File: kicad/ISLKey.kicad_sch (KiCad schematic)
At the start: 43 parts, among them J10 5-60V AC/DC IN, J11 12V OUT (lock/aux), J13 TTGO batt pads, J3 Exit btn, J4 Door contact, J5 Tamper, J6 LOCK COM/NO/NC, J7 AUX COM/NO/NC, J8 Fire volt-free, J9 Fire link COM-Fire, K1 SRD-05VDC-SL-C, K2 SRD-05VDC-SL-C, M1 TTGO T-Display, Q1 PN2222A, Q2 PN2222A, U1 PC817, U3 TEN20-2412WIN, U4 TSR-1-2450, U5 DS3231M

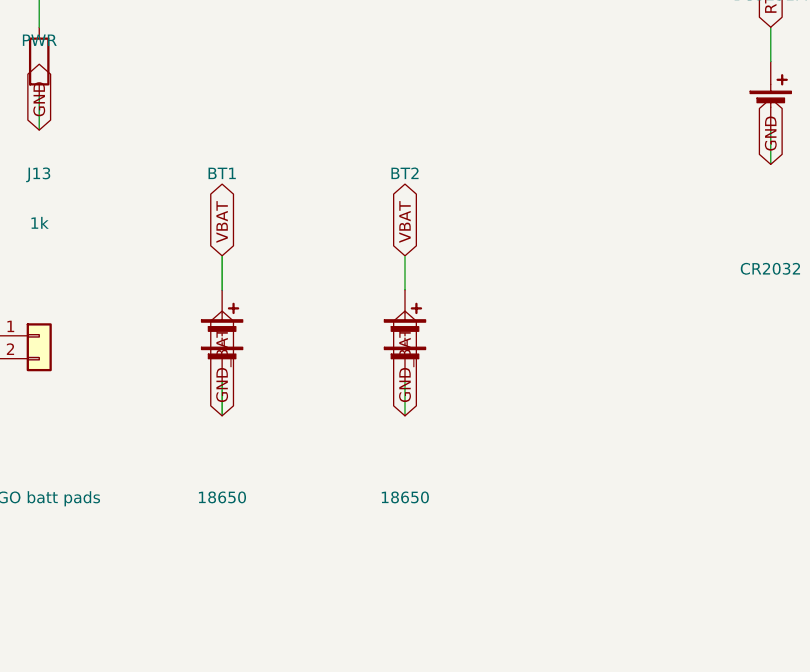
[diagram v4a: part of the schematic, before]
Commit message: kicad: single 18650 backup cell (was 2x)
Drop to one Keystone 1042 18650 holder (BT1) on VBAT/GND_BAT -> 3.7V straight
to the TTGO LiPo input (no series/parallel question, ~3000mAh covers the 7h
backup target). Board 140.9x132mm.

Co-Authored-By: Claude Opus 4.8 <noreply@anthropic.com>
Claude-Session: https://claude.ai/code/session_01WaJbCVpNNC7xF4fkqWpjpA
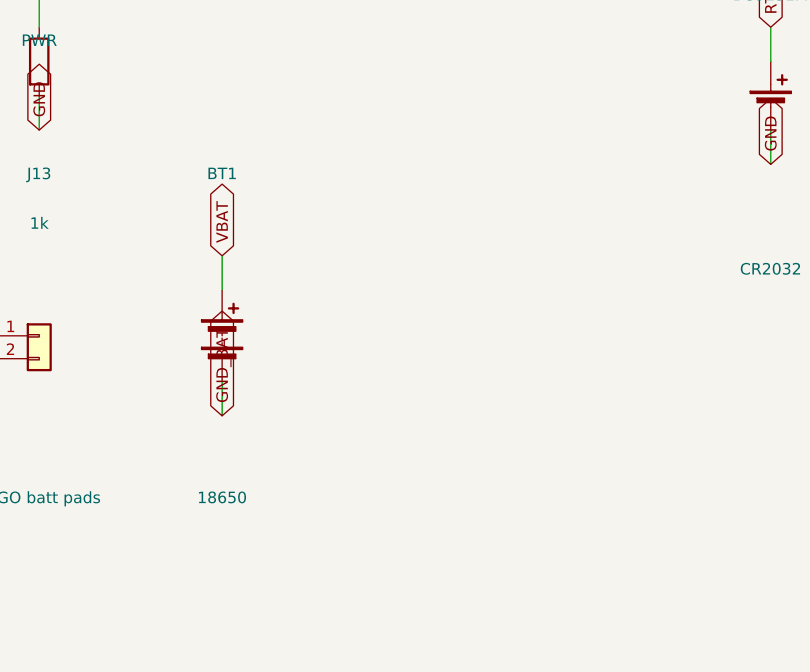
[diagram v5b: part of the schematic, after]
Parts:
- removed BT2: 18650, Battery:BatteryHolder_Keystone_1042_1x18650, symbol Device:Battery

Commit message: kicad: SMD passives, perimeter terminals, fully routed on user's placement
- Passives -> SMD (assembly-house placeable): R/LED 0805, ceramics 0805,
  flyback diodes SMA, electrolytics SMD alu (100V bulk on 10mm can).
- Fixed the Traco TEN20 footprint's buggy 51mm courtyard -> local
  lib/ISLKey.pretty/TEN20_TRACO (~26mm).
- User hand-placed the board in KiCad (terminals on the perimeter, USB-C
  clear, ~1/3 smaller). Repaired the malformed outline into a clean rect
  enclosing the corner mounting holes (148x128mm), redrew GND pours.
- Routed with Freerouting exporting the DSN WITHOUT the pour so GND routes
  as traces (avoids isolated pour-island unconnects): 368 traces + 22 vias,
  0 unrouted. DRC clean bar cosmetic silk-over-copper + text-height.

NOTE: ISLKey.kicad_pcb is now hand-placed + routed; do NOT re-run make_pcb.py
(it regenerates placement from scratch and would wipe this).

Co-Authored-By: Claude Opus 4.8 <noreply@anthropic.com>
Claude-Session: https://claude.ai/code/session_01WaJbCVpNNC7xF4fkqWpjpA
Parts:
- C1, C5: footprint Capacitor_THT:CP_Radial_D6.3mm_P2.50mm -> Capacitor_SMD:CP_Elec_6.3x5.3
- C2, C3, C6: footprint Capacitor_THT:C_Disc_D5.0mm_W2.5mm_P5.00mm -> Capacitor_SMD:C_0805_2012Metric
- C4: footprint Capacitor_THT:CP_Radial_D6.3mm_P2.50mm -> Capacitor_SMD:CP_Elec_10x10.5
- D1, D2: footprint Diode_THT:D_DO-41_SOD81_P10.16mm_Horizontal -> Diode_SMD:D_SMA
- D3, D4, D5: footprint LED_THT:LED_D3.0mm -> LED_SMD:LED_0805_2012Metric
- R1, R2, R3, R4, R5, R6, R7, R8: footprint Resistor_THT:R_Axial_DIN0207_L6.3mm_D2.5mm_P7.62mm_Horizontal -> Resistor_SMD:R_0805_2012Metric
- U3: footprint Converter_DCDC:Converter_DCDC_TRACO_TEN20-xxxx_THT -> ISLKey:TEN20_TRACO

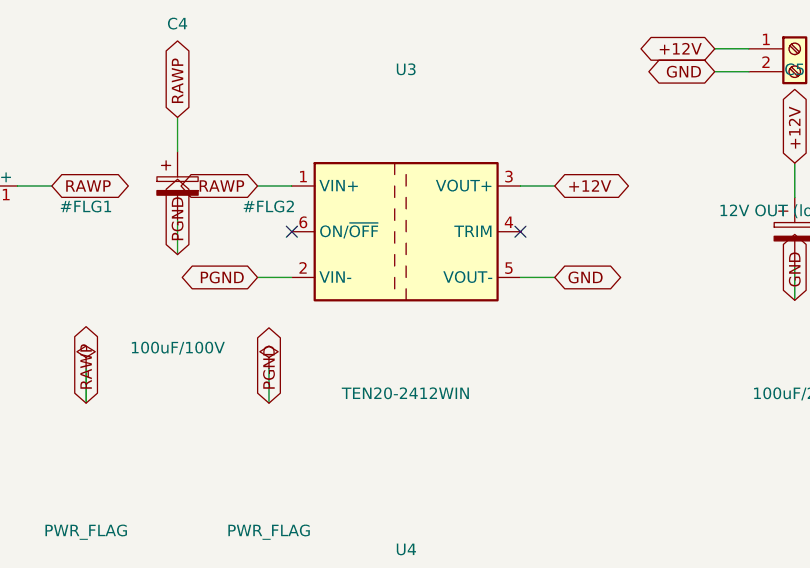
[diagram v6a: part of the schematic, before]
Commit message: kicad: swap isolated DC-DC to Traco TMR10-2412WIR (was TEN20, too big)
TEN20-2412WIN (25.4x25.4mm 20W 1"x1" brick) -> TMR10-2412WIR (13.7x23.6mm,
10W, 9-36V->isolated 12V) -- ~half the area, powers logic + a ~6W lock.
Rewired U3 (1=-Vin/PGND, 2=+Vin/RAWP, 3=Remote NC=on, 6=+Vout/12V,
7=-Vout/GND, 9/10=Case NC). Footprint swapped in place on the hand-placed
board, re-routed (GND-as-traces): 328 traces + 25 vias, DRC clean bar
cosmetic silk text-height.

Co-Authored-By: Claude Opus 4.8 <noreply@anthropic.com>
Claude-Session: https://claude.ai/code/session_01WaJbCVpNNC7xF4fkqWpjpA
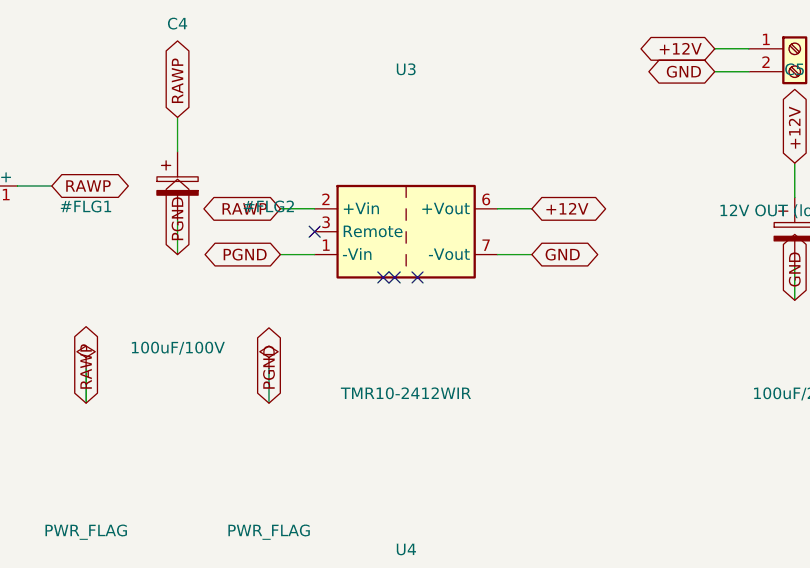
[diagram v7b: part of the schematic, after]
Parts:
- removed U3: TEN20-2412WIN, ISLKey:TEN20_TRACO, symbol Converter_DCDC:TEN20-2411WIN
- added U3: TMR10-2412WIR, Converter_DCDC:Converter_DCDC_TRACO_TMR10-24xxWIR_48xxWIR_72xxWIR_THT, symbol Converter_DCDC:TMR10-2410WIR
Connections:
- net +12V: now also U3.6 (+Vout)
- net GND: now also U3.7 (-Vout)
- net PGND: now also U3.1 (-Vin)
- net RAWP: now also U3.2 (+Vin)
- no-connect marks 13 -> 15

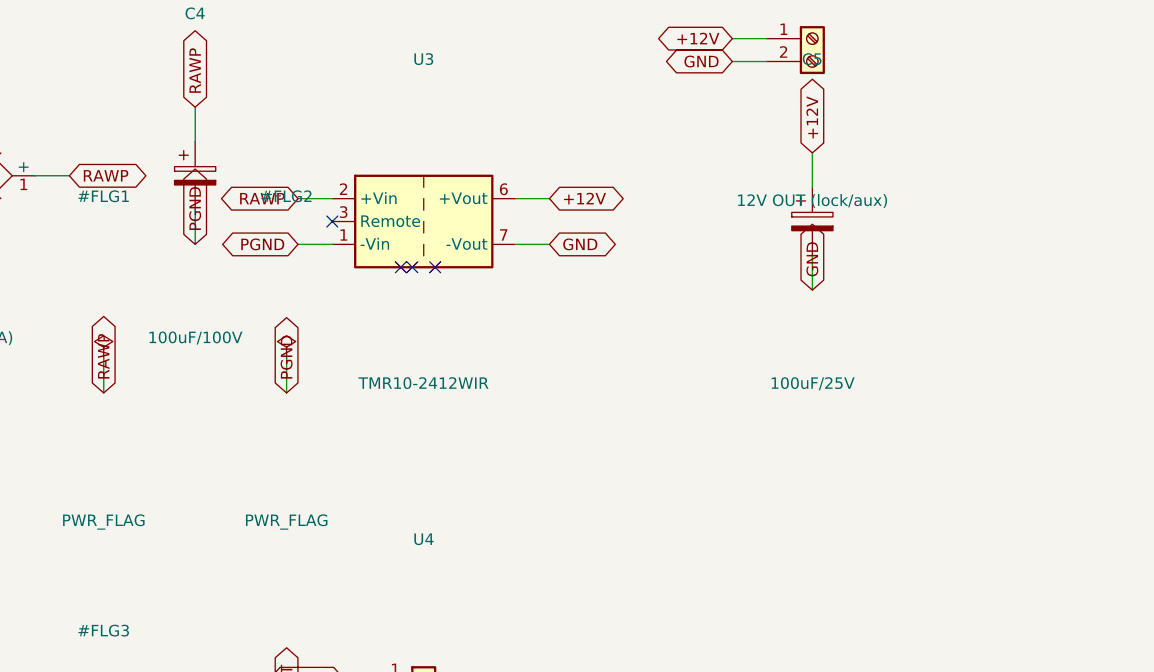
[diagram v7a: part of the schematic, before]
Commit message: kicad: add TMR10 Ctrl/Remote enable jumper (J15)
2-pin jumper J15 links U3 pin3 (Ctrl/Remote, net DCDC_CTRL) to +Vin (RAWP):
fit the shunt to tie Ctrl->+Vin (forces ON regardless of the module's logic
polarity); leave open = ON for positive-logic parts. Placed in the space
freed by the smaller TMR10; re-routed (356 traces + 26 vias, DRC clean bar
cosmetic silk).

Co-Authored-By: Claude Opus 4.8 <noreply@anthropic.com>
Claude-Session: https://claude.ai/code/session_01WaJbCVpNNC7xF4fkqWpjpA
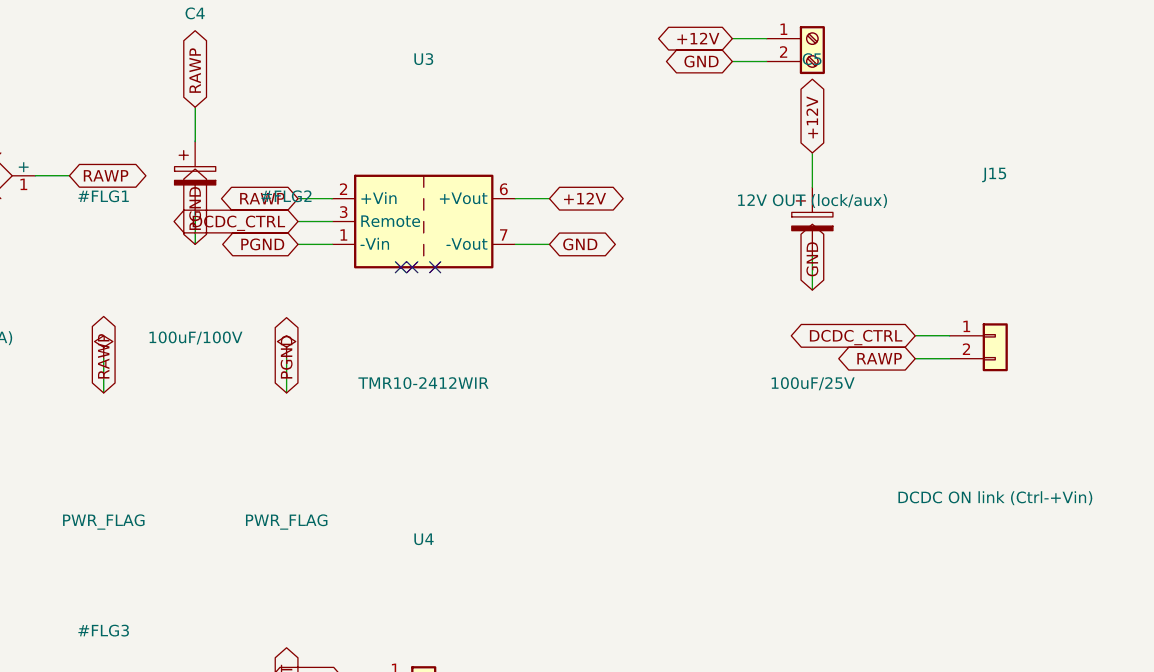
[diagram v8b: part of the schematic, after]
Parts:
- added J15: DCDC ON link (Ctrl-+Vin), Connector_PinHeader_2.54mm:PinHeader_1x02_P2.54mm_Vertical, symbol Connector_Generic:Conn_01x02
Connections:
- net RAWP: now also J15.2 (Pin_2)
- net DCDC_CTRL: now reaches U3.3 (Remote)
- net DCDC_CTRL: now also J15.1 (Pin_1)
- no-connect marks 15 -> 14
